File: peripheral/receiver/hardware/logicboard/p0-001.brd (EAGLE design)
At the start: 23 x 72 mm, 23 parts, among them IC1 74LS07N, IC2 LTC485N, IC3 LTC485N

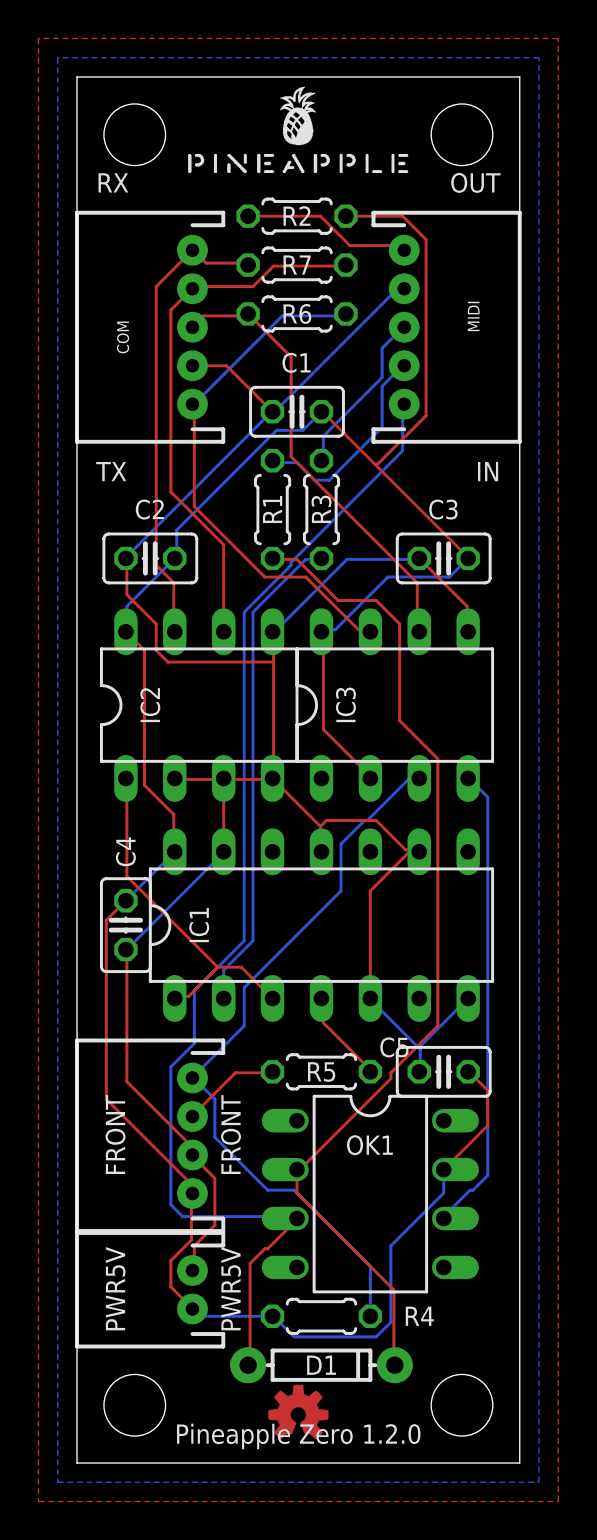
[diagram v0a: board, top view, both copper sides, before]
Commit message: Added DX receiver.
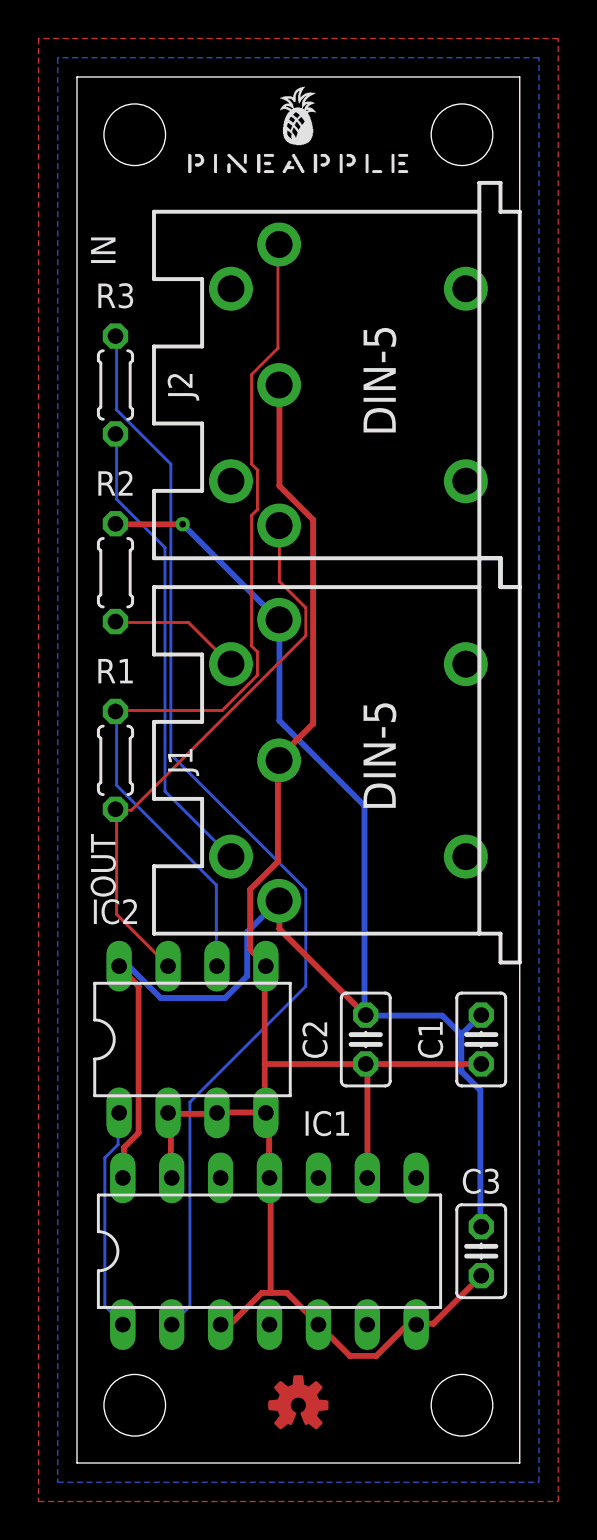
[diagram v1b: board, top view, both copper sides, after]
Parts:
- removed C4, C5: 103, rcl:C025-025X050
- removed COM, MIDI: (no value), SparkFun-Connectors:JST-5-PTH
- removed D1: (no value), SparkFun-DiscreteSemi:DIODE-1N4148
- removed FRONT: (no value), SparkFun-Connectors:JST-4-PTH
- removed IC3: LTC485N, linear-technology:DIL08
- removed OK1: 6N137, optocoupler:DIL08
- removed PWR5V: (no value), SparkFun-Connectors:JST-2-PTH
- removed R4: 10k, resistor:0204/5
- removed R5: 330, resistor:0204/5
- removed R6, R7: 120, resistor:0204/5
- added J1, J2: DIN5, SparkFun-Connectors:DIN5-RA-PTH
- R1: value 220 -> 120
- moved C3 36.0 mm to (21.0, 11.0), turned to 270 degrees
- moved C1 34.0 mm to (21.0, 22.0), turned to 270 degrees
- moved C2 27.4 mm to (15.0, 22.0), turned to 270 degrees
- moved R2 20.8 mm to (2.00, 46.2), turned to 90 degrees
- moved IC2 17.4 mm to (6.00, 22.0)
- moved IC1 17.2 mm to (10.0, 11.0)
- moved R1 15.4 mm to (2.00, 36.5)
- moved R3 12.5 mm to (2.00, 56.0)
- moved LOGO1 0.50 mm to (11.5, 3.00)
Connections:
- removed net IND: IC1.4, R5.2
- removed net INDR: FRONT.3, R5.1
- removed net MIDIIN: IC3.4, OK1.6
- removed net MIDIIN+: MIDI.4, R1.2
- removed net MIDIIN-: D1.A, MIDI.5, OK1.3
- removed net MIDIINA: D1.C, OK1.2, R1.1
- removed net MIDIOUT: IC1.1, IC1.3, IC2.1
- removed net MIDIOUT+: MIDI.1, R2.1
- removed net MIDIOUT-: MIDI.3, R3.2
- removed net MIDIOUT-RAW: IC1.2, R3.1
- removed net TX+: COM.3, IC3.6, R6.2
- removed net TX-: COM.1, IC3.7, R6.1
- removed net TXMUTE: FRONT.4, IC3.3, R4.2
- new net MOUTRTN: J1.5, R3.1
- new net MOUTSND: J1.4, R2.1
- new net N$1: IC1.2, R3.2
- new net TX: IC1.1, IC2.1
- net GND: now also IC1.3, J1.2, J2.2; no longer C4.2, C5.2, COM.2, FRONT.2, IC3.5, MIDI.2, PWR5V.2
- net RX+: now also J2.1, R1.2; no longer COM.4, R7.2
- net RX-: now also J2.3, R1.1; no longer COM.5, R7.1
- net VCC: now also J1.1, J1.3; no longer C4.1, C5.1, FRONT.1, IC3.2, IC3.8, OK1.7, PWR5V.1, R4.1
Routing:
- net MIDIIN-: track 62.3 -> 0.00 mm
- net N$1: track 0.00 -> 58.3 mm
- net MIDIINA: track 52.8 -> 0.00 mm
- net VCC: track 129.8 -> 82.2 mm, vias 0 -> 1
- net TXMUTE: track 37.8 -> 0.00 mm
- net GND: track 122.7 -> 92.8 mm
- net TX-: track 27.2 -> 0.00 mm
- net MIDIOUT-RAW: track 25.4 -> 0.00 mm
- net MOUTRTN: track 0.00 -> 24.5 mm
- net MIDIIN: track 24.3 -> 0.00 mm
- net TX+: track 23.4 -> 0.00 mm
- net RX+: track 27.9 -> 46.9 mm
- net MIDIOUT: track 18.2 -> 0.00 mm
- net TX: track 0.00 -> 11.7 mm
- net MIDIIN+: track 11.0 -> 0.00 mm
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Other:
- board text removed: "FRONT"
- board text removed: "PWR5V"
- board text removed: "Pineapple Zero 1.2.0"
- board text removed: "RX"
- board text removed: "TX"

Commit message: Alternative Qi connectors.
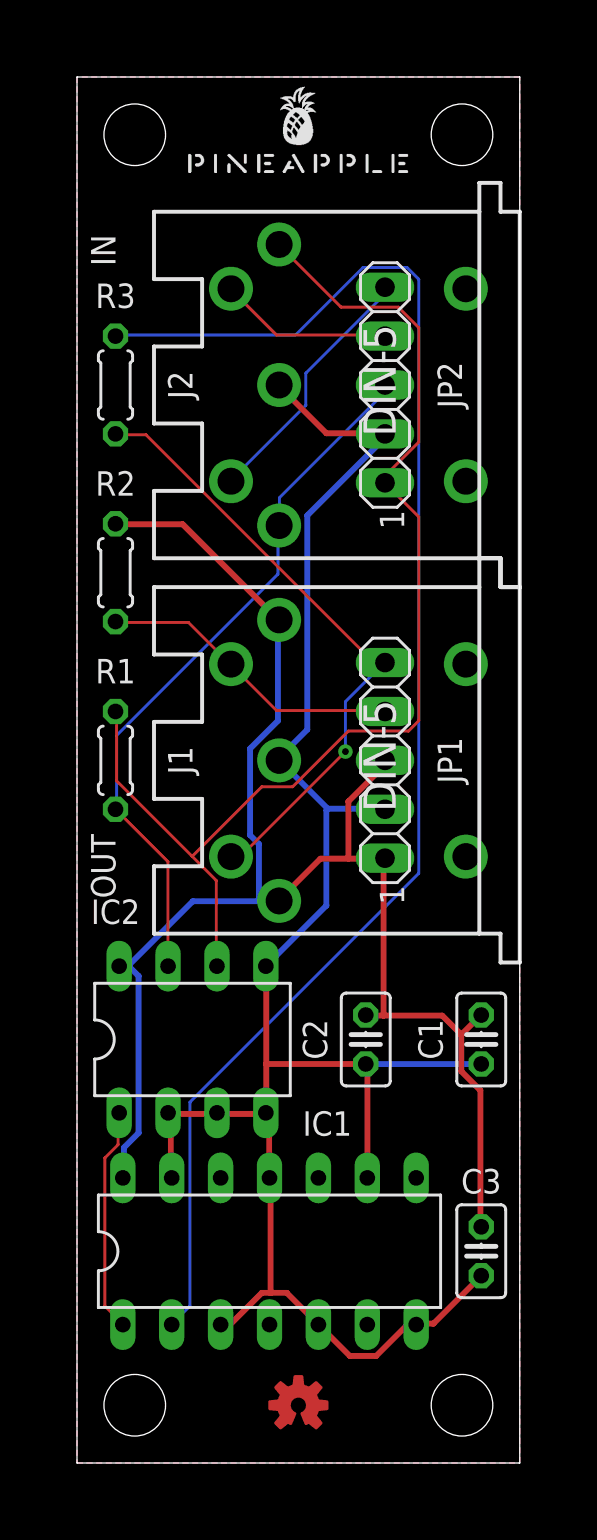
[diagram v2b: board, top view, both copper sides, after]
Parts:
- added JP1, JP2: (no value), pinhead:1X05
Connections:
- new net DUMMY4: J2.4, JP2.4
- new net DUMMY5: J2.5, JP2.5
- net GND: now also JP1.2, JP2.2
- net MOUTRTN: now also JP1.5
- net MOUTSND: now also JP1.4
- net RX+: now also JP2.1
- net RX-: now also JP2.3
- net VCC: now also JP1.1, JP1.3
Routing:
- net N$1: track 58.3 -> 77.1 mm
- net RX+: track 46.9 -> 61.1 mm
- net DUMMY5: track 0.00 -> 13.4 mm
- net GND: track 92.8 -> 102.0 mm
- net MOUTSND: track 6.91 -> 15.9 mm
- net DUMMY4: track 0.00 -> 9.04 mm
- net MOUTRTN: track 24.5 -> 32.6 mm, vias 0 -> 1
- net RX-: track 29.2 -> 37.2 mm
- net VCC: track 82.2 -> 86.5 mm, vias 1 -> 0
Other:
- board text added: "1"
